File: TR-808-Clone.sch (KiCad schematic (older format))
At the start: 601 parts, among them J1 BD, J10 OH, J11 CH, J12 MASTER, J2 SD, J3 LT, J4 MT, J5 HT, J6 RS, J7 CP, J8 CB, J9 CY, P1 CONN_02X05, P10 CONN_01X01, P11 CONN_01X01, P2 CONN_01X08, P4 CONN_01X01, P5 CONN_01X01, P8 CONN_01X01, P9 CONN_01X01, Q10 A733, Q11 C945, Q12 A733, Q13 J111/J112, Q27-1 C945, Q28 C945, Q29 A733, Q31 C945, Q32 C945, Q33 C945, Q34 C945, Q35 C945, Q36 C945, Q37 A733, Q39 C945, Q40 A733, Q41 C945, Q42 C945, Q43 C945, Q44 C945, Q45 C945, Q46 A733, Q47 C945, Q48 C945, Q49 C945, Q50 C945, Q51 A733, Q52 C945, Q53 C945, Q54 A733, Q55 C945, Q56 C945, Q57 A733, Q58 C945, Q59 C945, Q60 A733, Q61 C945, Q62 C945, Q63 C945, Q65 A733, Q66 A733, Q67 C945, Q68 C945, Q69 C945, Q70 C945, Q71 A733, Q72 A733, Q73 C945, Q74 J111/J112, U10 CD4053, U11 CD4053, U12 4558, U13 4558, U14 4558, U15 4558, U16 4558, U17 4558, U18 4558, U19 4558, U20 4558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

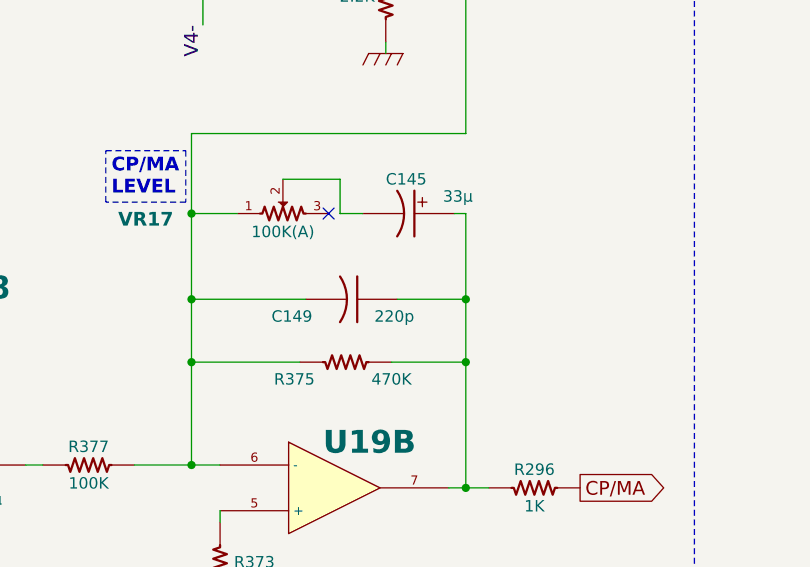
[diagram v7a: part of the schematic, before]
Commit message: more manual work, about to resize front panel diagram to A4
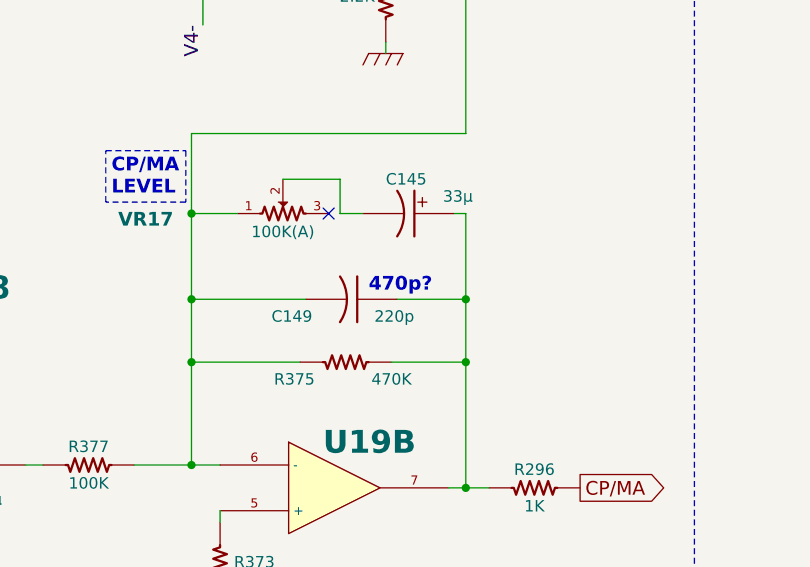
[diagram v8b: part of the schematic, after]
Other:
- note added: "470p?"
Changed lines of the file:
@@
 Wire Wire Line
 	17300 15650 17400 15650
+Text Notes 9200 21350 0    60   ~ 12
+470p?
 $EndSCHEMATC
